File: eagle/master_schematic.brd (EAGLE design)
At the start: 160 x 100 mm, 103 parts

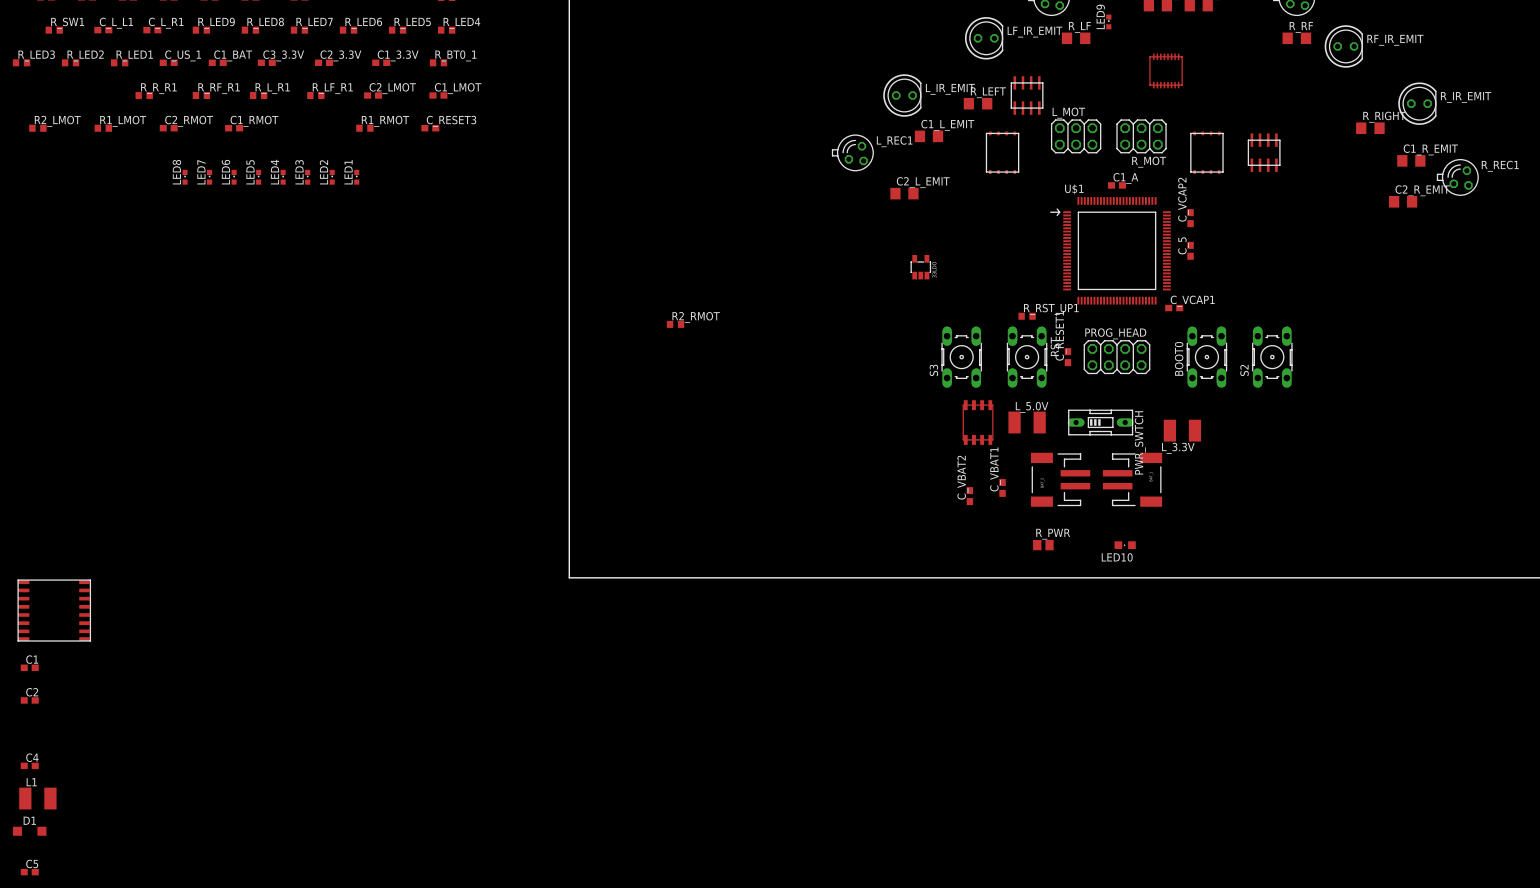
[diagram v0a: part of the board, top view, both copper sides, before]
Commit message: Added Buzzer
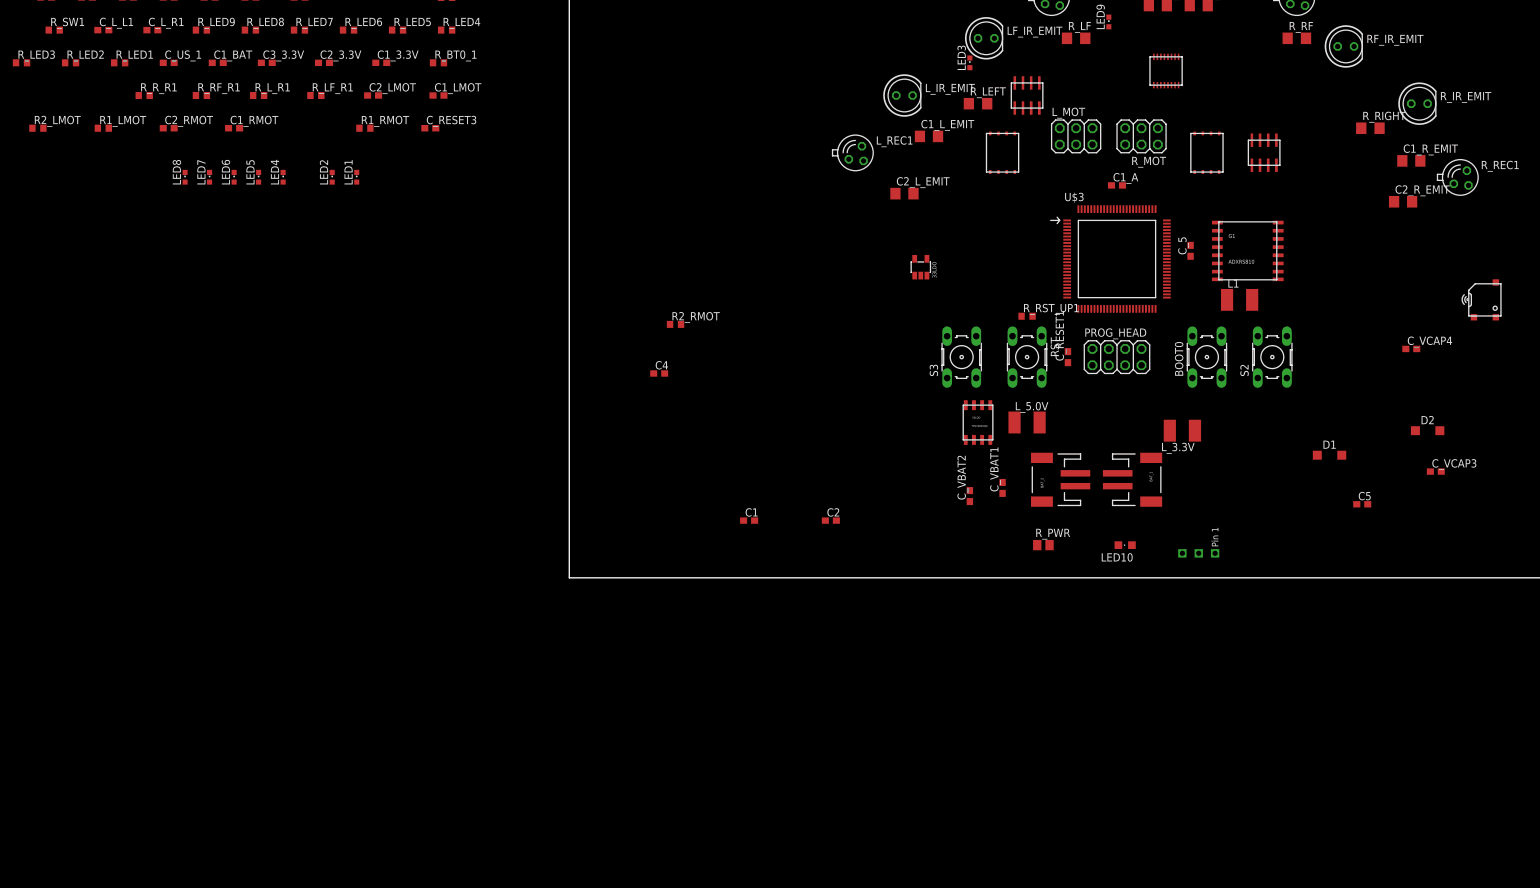
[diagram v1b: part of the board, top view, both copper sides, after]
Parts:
- removed C_VCAP1, C_VCAP2: 2.2uF, rcl:C0603
- removed PWR_SWTCH: (no value), special:EDG-01
- removed U$1: STM32F767VG(2), MCU:LQFP100
- added C_VCAP3, C_VCAP4: 2.2uF, rcl:C0603
- added D2: 25V, diode:SOD123
- added SPK1: SMT-0540-S-R, SMT-0540-S-R:SMT-0540-S-R
- added U$2: T212031, GCswitch:T212031
- added U$3: STM32F769VG-1, MCU:LQFP100
- L_MOT: value (none) -> L1
- R_MOT: value (none) -> R1
- moved C5 214.8 mm to (123.2, 11.4)
- moved D1 210.2 mm to (118.1, 19.1)
- moved L1 202.1 mm to (104.1, 43.2)
- moved G1 193.7 mm to (105.4, 50.8)
- moved C2 127.6 mm to (40.6, 8.89)
- moved C4 115.2 mm to (14.0, 31.8)
- moved C1 114.1 mm to (27.9, 8.89)
- moved LED3 104.4 mm to (62.2, 80.0)
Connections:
- removed net GYRO_CS: G1.4
- removed net LF_TX: U$1.5
- removed net LPWM: MOS_L.IN_A, R1_LMOT.2, U$1.23
- removed net L_TX: U$1.4
- removed net N$12: U$1.37
- removed net N$13: U$1.36
- removed net N$15: U$1.91
- removed net N$16: U$1.24
- removed net N$3: C_VCAP2.1, U$1.73
- removed net N$4: C_VCAP1.1, U$1.48
- removed net N$7: U$1.92
- removed net RF_TX: U$1.55
- removed net R_TX: U$1.56
- removed net US_2: U$1.38
- new net BUZZER: U$3.59, U$4.1
- new net G_CS: G1.4, U$3.28
- new net LED10: U$3.46
- new net LPWMA: MOS_L.IN_A, R1_LMOT.2, U$3.24
- new net N$14: D1.A, G1.8, L1.2
- new net N$29: D2.A, SPK1.+, U$4.16
- new net N$56: C_VCAP4.1, U$3.73
- new net N$57: C_VCAP3.1, U$3.48
- new net SW1: U$3.63
- new net SW2: U$3.62
- new net SW3: U$3.61
- new net SW4: U$3.60
- new net VOLTMETER: U$3.15
- net 3.3V: now also D2.C, SPK1.-, U$3.100, U$3.11, U$3.27, U$3.50, U$3.6, U$3.75; no longer U$1.100, U$1.11, U$1.27, U$1.50, U$1.6, U$1.75
- net A3.3V: now also U$3.20, U$3.21; no longer U$1.20, U$1.21
- net BOOT0: now also U$3.94; no longer U$1.94
- net GND: now also C_VCAP3.2, C_VCAP4.2, U$3.10, U$3.19, U$3.26, U$3.49, U$3.74, U$3.99; no longer C_VCAP1.2, C_VCAP2.2, U$1.10, U$1.19, U$1.26, U$1.49, U$1.74, U$1.99
- net G_MISO: now also U$3.30
- net G_MOSI: now also U$3.31
- net G_SCLK: now also U$3.29
- net LED1: now also U$3.51; no longer U$1.85
- net LED2: now also U$3.52; no longer U$1.41
- net LED3: now also U$3.53; no longer U$1.42
- net LED4: now also U$3.17; no longer U$1.82
- net LED5: now also U$3.16; no longer U$1.83
- net LED6: now also U$3.85; no longer U$1.84
- net LED7: now also U$3.84; no longer U$1.53
- net LED8: now also U$3.83; no longer U$1.52
- net LED9: now also U$3.82; no longer U$1.51
- net LEFT_REC: now also U$3.32; no longer U$1.30
- net LF_EMITTER: now also U$3.90
- net LF_REC: now also U$3.33; no longer U$1.33
- net LPWMB: now also U$3.25
- net L_EMITTER: now also U$3.91
- net L_ENC_A: now also U$3.41; no longer U$1.1
- net L_ENC_B: now also U$3.39; no longer U$1.2
- net N$20: now also D1.C; no longer G1.8, L1.2
- net N$31: now also U$2.2; no longer PWR_SWTCH.2
- net RESET: now also U$3.14; no longer U$1.14
- net RF_EMITTER: now also U$3.66
- net RF_REC: now also U$3.34; no longer U$1.32
- net RIGHT_REC: now also U$3.35; no longer U$1.31
- net RPWMA: now also U$3.22
- net RPWMB: now also U$3.23
- net RX: now also U$3.69; no longer U$1.69
- net R_EMITTER: now also U$3.65
- net R_ENC_A: now also U$3.44; no longer U$1.65
- net R_ENC_B: now also U$3.43; no longer U$1.66
- net SWCLK: now also U$3.76; no longer U$1.76
- net SWDIO: now also U$3.72; no longer U$1.72
- net TX: now also U$3.68; no longer U$1.68
- net US_1: no longer U$1.39
- net V_BAT: now also U$2.3; no longer PWR_SWTCH.1
